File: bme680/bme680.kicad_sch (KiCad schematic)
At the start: 0 parts

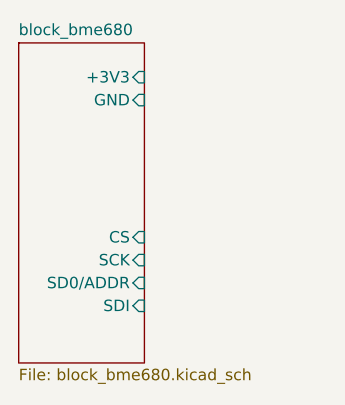
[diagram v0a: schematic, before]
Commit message: bug fixes in BME680
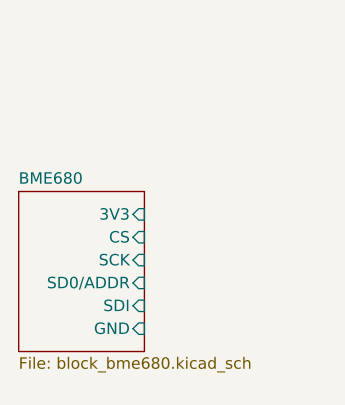
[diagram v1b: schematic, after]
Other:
- sheet block_bme680 renamed BME680
- sheet BME680 ports: added 3V3; removed +3V3
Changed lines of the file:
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@@
 	(paper "A4")
 	(sheet
-		(at 105.41 66.04)
-		(size 13.97 35.56)
+		(at 105.41 82.55)
+		(size 13.97 17.78)
 		(exclude_from_sim no)
 		(in_bom yes)
@@
 			(color 0 0 0 0.0000)
 		)
-		(property "Sheetname" "block_bme680"
-			(at 105.41 65.3284 0)
+		(property "Sheetname" "BME680"
+			(at 105.41 81.8384 0)
 			(effects
 				(font
@@
 		)
 		(property "Sheetfile" "block_bme680.kicad_sch"
-			(at 105.41 102.1846 0)
+			(at 105.41 100.9146 0)
 			(effects
 				(font
@@
 			)
 		)
-		(pin "+3V3" input
-			(at 119.38 69.85 0)
+		(pin "3V3" input
+			(at 119.38 85.09 0)
 			(effects
 				(font
@@
 		)
 		(pin "GND" input
-			(at 119.38 72.39 0)
+			(at 119.38 97.79 0)
 			(effects
 				(font
